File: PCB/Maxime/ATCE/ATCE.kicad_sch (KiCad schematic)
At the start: 12 parts, among them U1 ATmega32U4-A, U2 TL081, Y1 Crystal

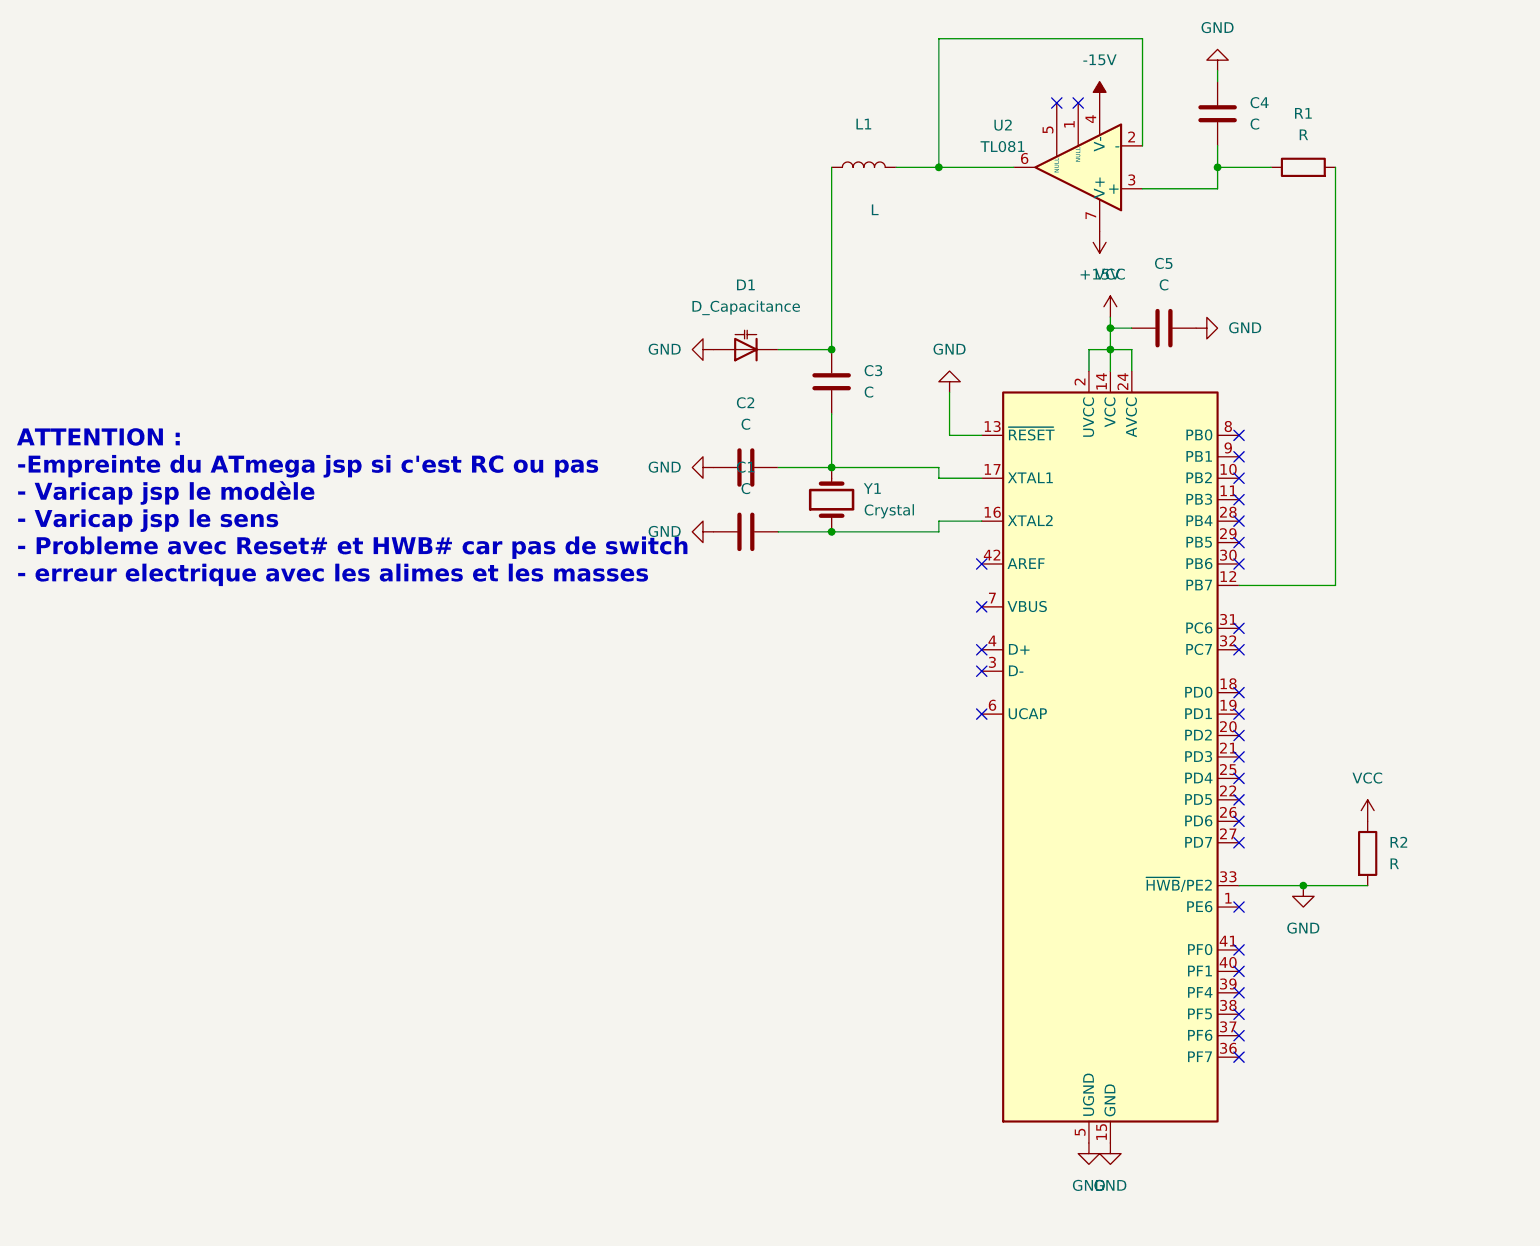
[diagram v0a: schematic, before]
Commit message: correction des erreurs electriques
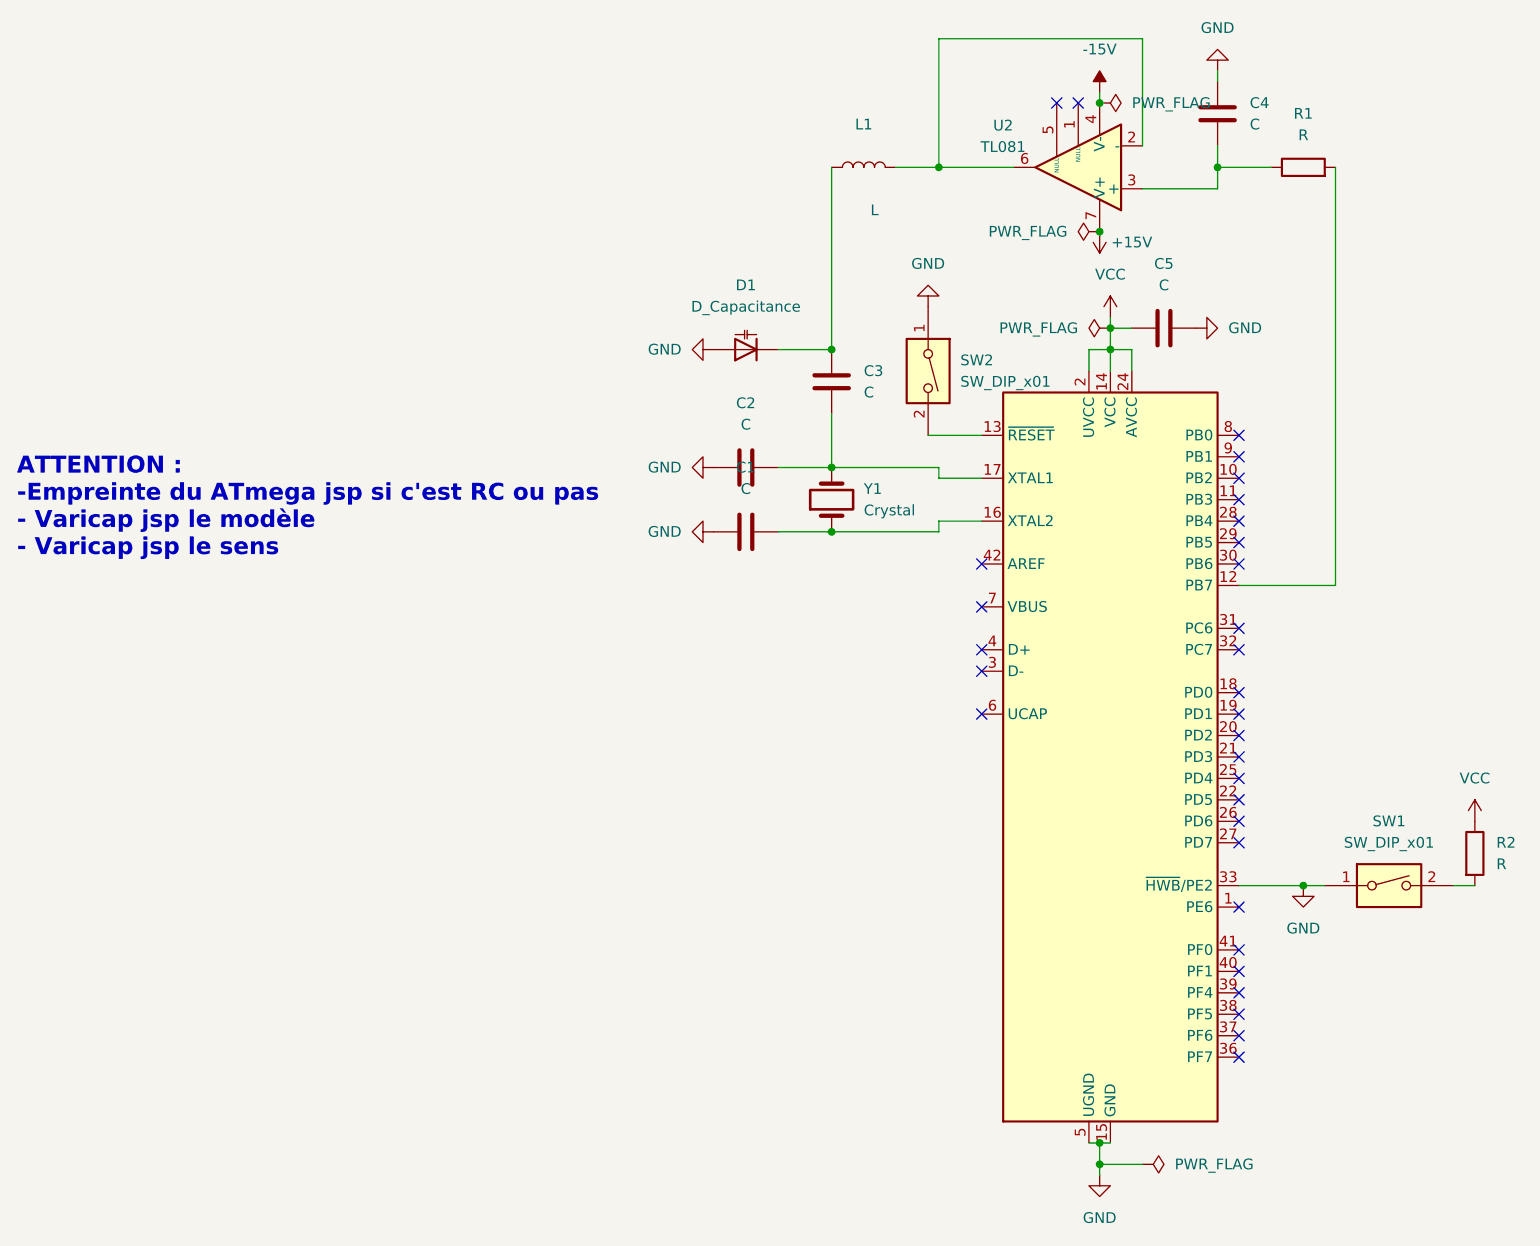
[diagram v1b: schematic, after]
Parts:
- added SW1, SW2: SW_DIP_x01, symbol Switch:SW_DIP_x01
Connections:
- net GND: now also SW1.1, SW2.1; no longer R2.2, U1.13 (~{RESET})
- new net: SW2.2, U1.13 (~{RESET})
- new net: R2.2, SW1.2
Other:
- note added: "ATTENTION : -Empreinte du ATmega jsp si c'est RC ou pas - Varicap jsp le modèle - Varicap jsp le sens"
- note removed: "ATTENTION : -Empreinte du ATmega jsp si c'est RC ou pas - Varicap jsp le modèle - Varicap jsp le sens - Probleme avec Reset# et HWB# car pas de switch - erreur electrique avec les alimes et les masses"
- moved on the sheet: R2
